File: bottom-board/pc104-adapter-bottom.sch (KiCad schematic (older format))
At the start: 12 parts, among them J1 Conn_01x13_Male, J10 SAMTEC-TSW-126-07-X-D, J2 Conn_01x13_Male, J3 Conn_01x13_Male, J4 Conn_01x13_Male, J5 Conn_01x13_Male, J6 Conn_01x13_Male, J7 Conn_01x13_Male, J8 Conn_01x13_Male, J9 SAMTEC-TSW-126-07-X-D

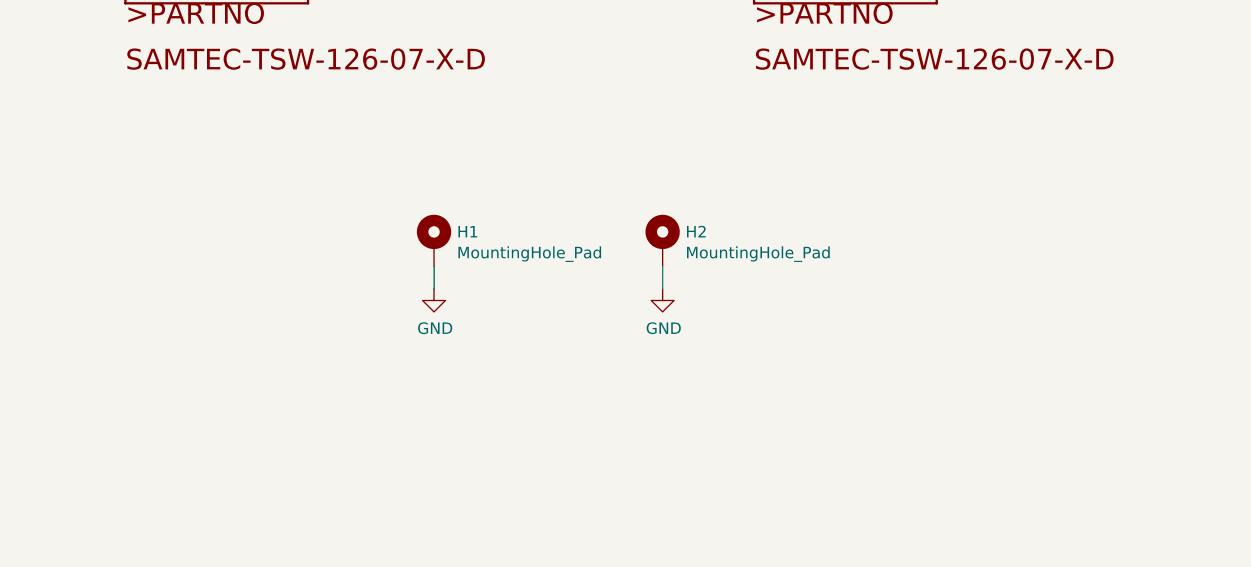
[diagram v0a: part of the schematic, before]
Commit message: bottom-board: schematic: Adding screw holes #13
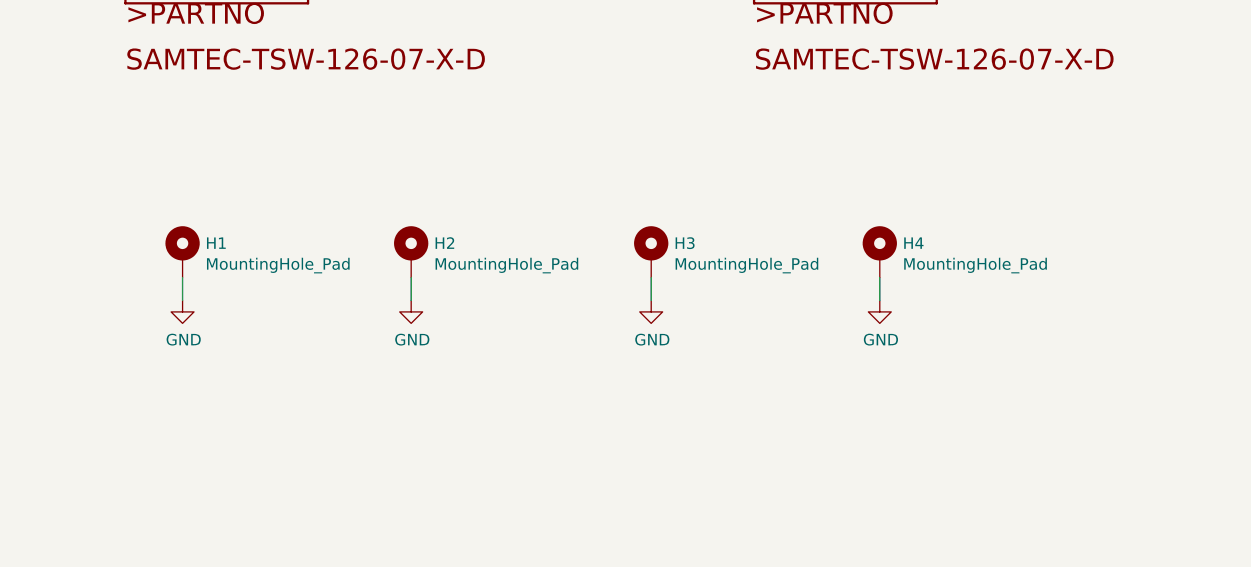
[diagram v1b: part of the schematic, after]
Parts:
- added H3, H4: MountingHole_Pad, MountingHole:MountingHole_3.2mm_M3_ISO14580_Pad, symbol Mechanical:MountingHole_Pad
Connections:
- net GND: now also H3.1, H4.1
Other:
- moved on the sheet: H1, H2
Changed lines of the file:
@@
 Sheet 1 1
 Title "PC-104 to PicoBlade Adapter (Bottom)"
-Date "2020-06-21"
-Rev "v1.0"
+Date "2020-08-03"
+Rev "v2.0"
 Comp "SpaceLab"
 Comment1 "Author: Gabriel Mariano Marcelino"
@@
 L Mechanical:MountingHole_Pad H1
 U 1 1 5F59E490
-P 7450 5250
-F 0 "H1" H 7550 5299 50  0000 L CNN
-F 1 "MountingHole_Pad" H 7550 5208 50  0000 L CNN
-F 2 "MountingHole:MountingHole_3.2mm_M3_ISO14580_Pad" H 7450 5250 50  0001 C CNN
-F 3 "~" H 7450 5250 50  0001 C CNN
-	1    7450 5250
+P 6350 5300
+F 0 "H1" H 6450 5349 50  0000 L CNN
+F 1 "MountingHole_Pad" H 6450 5258 50  0000 L CNN
+F 2 "MountingHole:MountingHole_3.2mm_M3_ISO14580_Pad" H 6350 5300 50  0001 C CNN
+F 3 "~" H 6350 5300 50  0001 C CNN
+	1    6350 5300
 	1    0    0    -1
 $EndComp
@@
 L Mechanical:MountingHole_Pad H2
 U 1 1 5F5A173F
-P 8450 5250
-F 0 "H2" H 8550 5299 50  0000 L CNN
-F 1 "MountingHole_Pad" H 8550 5208 50  0000 L CNN
-F 2 "MountingHole:MountingHole_3.2mm_M3_ISO14580_Pad" H 8450 5250 50  0001 C CNN
-F 3 "~" H 8450 5250 50  0001 C CNN
-	1    8450 5250
+P 7350 5300
+F 0 "H2" H 7450 5349 50  0000 L CNN
+F 1 "MountingHole_Pad" H 7450 5258 50  0000 L CNN
+F 2 "MountingHole:MountingHole_3.2mm_M3_ISO14580_Pad" H 7350 5300 50  0001 C CNN
+F 3 "~" H 7350 5300 50  0001 C CNN
+	1    7350 5300
 	1    0    0    -1
 $EndComp
@@
 L power:GND #PWR01
 U 1 1 5F5D55CB
-P 7450 5450
-F 0 "#PWR01" H 7450 5200 50  0001 C CNN
-F 1 "GND" H 7455 5277 50  0000 C CNN
-F 2 "" H 7450 5450 50  0001 C CNN
-F 3 "" H 7450 5450 50  0001 C CNN
-	1    7450 5450
+P 6350 5500
+F 0 "#PWR01" H 6350 5250 50  0001 C CNN
+F 1 "GND" H 6355 5327 50  0000 C CNN
+F 2 "" H 6350 5500 50  0001 C CNN
+F 3 "" H 6350 5500 50  0001 C CNN
+	1    6350 5500
 	1    0    0    -1
 $EndComp
@@
 L power:GND #PWR02
 U 1 1 5F5D6345
-P 8450 5450
-F 0 "#PWR02" H 8450 5200 50  0001 C CNN
-F 1 "GND" H 8455 5277 50  0000 C CNN
-F 2 "" H 8450 5450 50  0001 C CNN
-F 3 "" H 8450 5450 50  0001 C CNN
-	1    8450 5450
-	1    0    0    -1
-$EndComp
-Wire Wire Line
-	7450 5450 7450 5350
-Wire Wire Line
-	8450 5450 8450 5350
+P 7350 5500
+F 0 "#PWR02" H 7350 5250 50  0001 C CNN
+F 1 "GND" H 7355 5327 50  0000 C CNN
+F 2 "" H 7350 5500 50  0001 C CNN
+F 3 "" H 7350 5500 50  0001 C CNN
+	1    7350 5500
+	1    0    0    -1
+$EndComp
+Wire Wire Line
+	6350 5500 6350 5400
+Wire Wire Line
+	7350 5500 7350 5400
+$Comp
+L Mechanical:MountingHole_Pad H3
+U 1 1 5F29610C
+P 8400 5300
+F 0 "H3" H 8500 5349 50  0000 L CNN
+F 1 "MountingHole_Pad" H 8500 5258 50  0000 L CNN
+F 2 "MountingHole:MountingHole_3.2mm_M3_ISO14580_Pad" H 8400 5300 50  0001 C CNN
+F 3 "~" H 8400 5300 50  0001 C CNN
+	1    8400 5300
+	1    0    0    -1
+$EndComp
+$Comp
+L Mechanical:MountingHole_Pad H4
+U 1 1 5F296112
+P 9400 5300
+F 0 "H4" H 9500 5349 50  0000 L CNN
+F 1 "MountingHole_Pad" H 9500 5258 50  0000 L CNN
+F 2 "MountingHole:MountingHole_3.2mm_M3_ISO14580_Pad" H 9400 5300 50  0001 C CNN
+F 3 "~" H 9400 5300 50  0001 C CNN
+	1    9400 5300
+	1    0    0    -1
+$EndComp
+$Comp
+L power:GND #PWR0101
+U 1 1 5F296118
+P 8400 5500
+F 0 "#PWR0101" H 8400 5250 50  0001 C CNN
+F 1 "GND" H 8405 5327 50  0000 C CNN
+F 2 "" H 8400 5500 50  0001 C CNN
+F 3 "" H 8400 5500 50  0001 C CNN
+	1    8400 5500
+	1    0    0    -1
+$EndComp
+$Comp
+L power:GND #PWR0102
+U 1 1 5F29611E
+P 9400 5500
+F 0 "#PWR0102" H 9400 5250 50  0001 C CNN
+F 1 "GND" H 9405 5327 50  0000 C CNN
+F 2 "" H 9400 5500 50  0001 C CNN
+F 3 "" H 9400 5500 50  0001 C CNN
+	1    9400 5500
+	1    0    0    -1
+$EndComp
+Wire Wire Line
+	8400 5500 8400 5400
+Wire Wire Line
+	9400 5500 9400 5400
 $EndSCHEMATC
